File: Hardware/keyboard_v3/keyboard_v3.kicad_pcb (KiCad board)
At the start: 2 copper layers, 50 x 36 mm, 15 parts, among them J1 Conn_01x08_Male, SW1 SW_Push, SW2 SW_Push, SW3 SW_Push, SW4 SW_Push, U1 74HC14

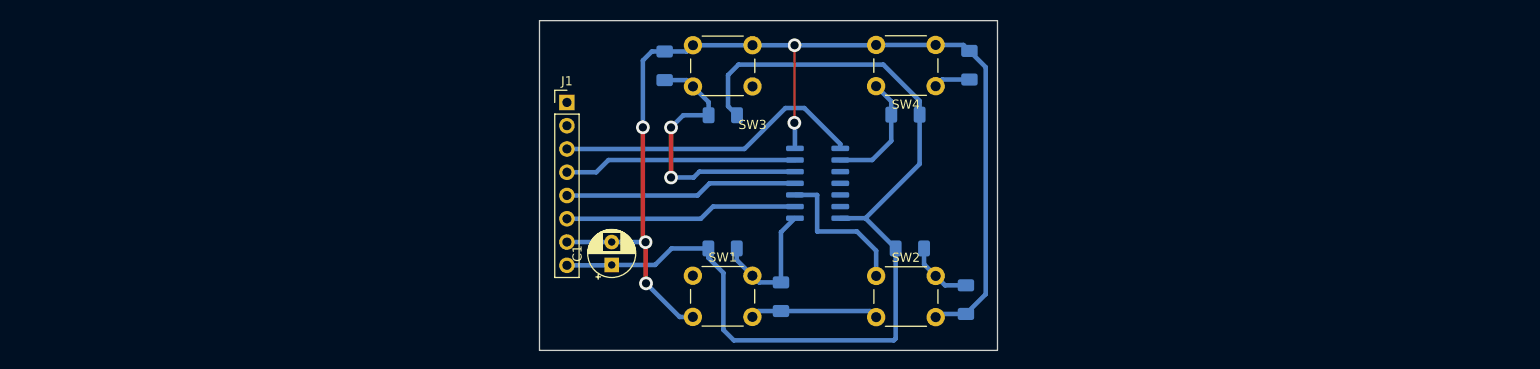
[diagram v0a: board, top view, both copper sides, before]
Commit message: Распаян и протестирован модуль клавиатуры keyboard_v3/. Можно приступить к доработке основного приложения
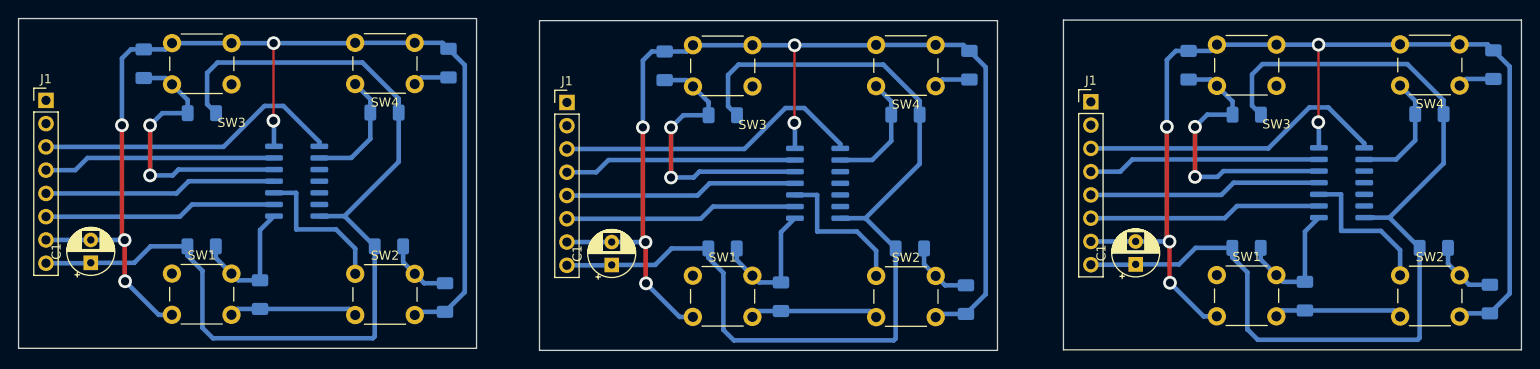
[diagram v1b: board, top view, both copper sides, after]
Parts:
- added C1: CP, Capacitor_THT:CP_Radial_D5.0mm_P2.50mm, F.Cu at (145.1, 96.6)
- added C1: CP, Capacitor_THT:CP_Radial_D5.0mm_P2.50mm, F.Cu at (31.0, 96.4)
- added C2: C, Capacitor_SMD:C_1206_3216Metric_Pad1.33x1.80mm_HandSolder, B.Cu at (163.6, 100.1)
- added C2: C, Capacitor_SMD:C_1206_3216Metric_Pad1.33x1.80mm_HandSolder, B.Cu at (49.5, 99.9)
- added C3: C, Capacitor_SMD:C_1206_3216Metric_Pad1.33x1.80mm_HandSolder, B.Cu at (183.8, 100.4)
- added C3: C, Capacitor_SMD:C_1206_3216Metric_Pad1.33x1.80mm_HandSolder, B.Cu at (69.7, 100.2)
- added C4: C, Capacitor_SMD:C_1206_3216Metric_Pad1.33x1.80mm_HandSolder, B.Cu at (150.9, 74.9)
- added C4: C, Capacitor_SMD:C_1206_3216Metric_Pad1.33x1.80mm_HandSolder, B.Cu at (36.8, 74.7)
- added C5: C, Capacitor_SMD:C_1206_3216Metric_Pad1.33x1.80mm_HandSolder, B.Cu at (184.1, 74.8)
- added C5: C, Capacitor_SMD:C_1206_3216Metric_Pad1.33x1.80mm_HandSolder, B.Cu at (70.1, 74.6)
- added J1: Conn_01x08_Male, Connector_PinHeader_2.54mm:PinHeader_1x08_P2.54mm_Vertical, F.Cu at (140.2, 78.9)
- added J1: Conn_01x08_Male, Connector_PinHeader_2.54mm:PinHeader_1x08_P2.54mm_Vertical, F.Cu at (26.1, 78.7)
- added R1: R, Resistor_SMD:R_1206_3216Metric_Pad1.30x1.75mm_HandSolder, B.Cu at (157.2, 94.8)
- added R1: R, Resistor_SMD:R_1206_3216Metric_Pad1.30x1.75mm_HandSolder, B.Cu at (43.1, 94.6)
- added R2: R, Resistor_SMD:R_1206_3216Metric_Pad1.30x1.75mm_HandSolder, B.Cu at (177.6, 94.8)
- added R2: R, Resistor_SMD:R_1206_3216Metric_Pad1.30x1.75mm_HandSolder, B.Cu at (63.6, 94.6)
- added R3: R, Resistor_SMD:R_1206_3216Metric_Pad1.30x1.75mm_HandSolder, B.Cu at (157.2, 80.3)
- added R3: R, Resistor_SMD:R_1206_3216Metric_Pad1.30x1.75mm_HandSolder, B.Cu at (43.1, 80.1)
- added R4: R, Resistor_SMD:R_1206_3216Metric_Pad1.30x1.75mm_HandSolder, B.Cu at (177.2, 80.2)
- added R4: R, Resistor_SMD:R_1206_3216Metric_Pad1.30x1.75mm_HandSolder, B.Cu at (63.1, 80.0)
- added SW1: SW_Push, Button_Switch_THT:SW_PUSH_6mm_H5mm, F.Cu at (157.2, 99.9)
- added SW1: SW_Push, Button_Switch_THT:SW_PUSH_6mm_H5mm, F.Cu at (43.1, 99.8)
- added SW2: SW_Push, Button_Switch_THT:SW_PUSH_6mm_H5mm, F.Cu at (177.2, 99.9)
- added SW2: SW_Push, Button_Switch_THT:SW_PUSH_6mm_H5mm, F.Cu at (63.1, 99.8)
- added SW3: SW_Push, Button_Switch_THT:SW_PUSH_6mm_H5mm, F.Cu at (157.2, 74.9)
- added SW3: SW_Push, Button_Switch_THT:SW_PUSH_6mm_H5mm, F.Cu at (43.1, 74.8)
- added SW4: SW_Push, Button_Switch_THT:SW_PUSH_6mm_H5mm, F.Cu at (177.2, 74.9)
- added SW4: SW_Push, Button_Switch_THT:SW_PUSH_6mm_H5mm, F.Cu at (63.1, 74.8)
- added U1: 74HC14, Package_SO:SOIC-14_3.9x8.7mm_P1.27mm, B.Cu at (167.6, 87.7)
- added U1: 74HC14, Package_SO:SOIC-14_3.9x8.7mm_P1.27mm, B.Cu at (53.5, 87.5)
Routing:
- net (no net): track 0.00 -> 877.1 mm, vias 0 -> 14
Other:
- board size 50 x 36 mm -> 164.1 x 36.2 mm
